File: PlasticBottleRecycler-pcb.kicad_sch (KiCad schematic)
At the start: 31 parts, among them J1 SWIM, J2 LCD, J3 Screw_Terminal_01x04, J4 NTC, J5 HEATER, J6 FAN1, J7 +12V, J8 +5V, Q1 IRF3205, Q2 BC337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

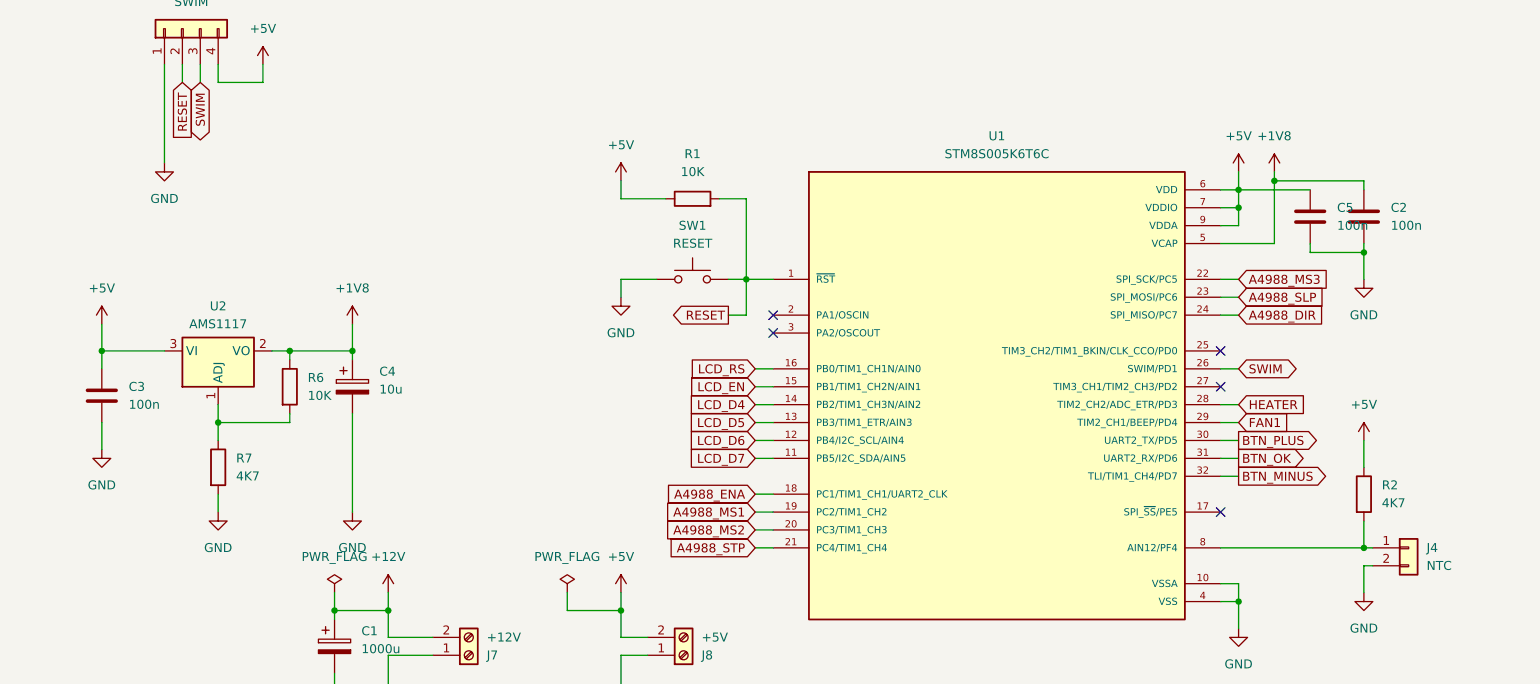
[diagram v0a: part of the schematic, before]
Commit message: Remove unnecesary voltage regulator
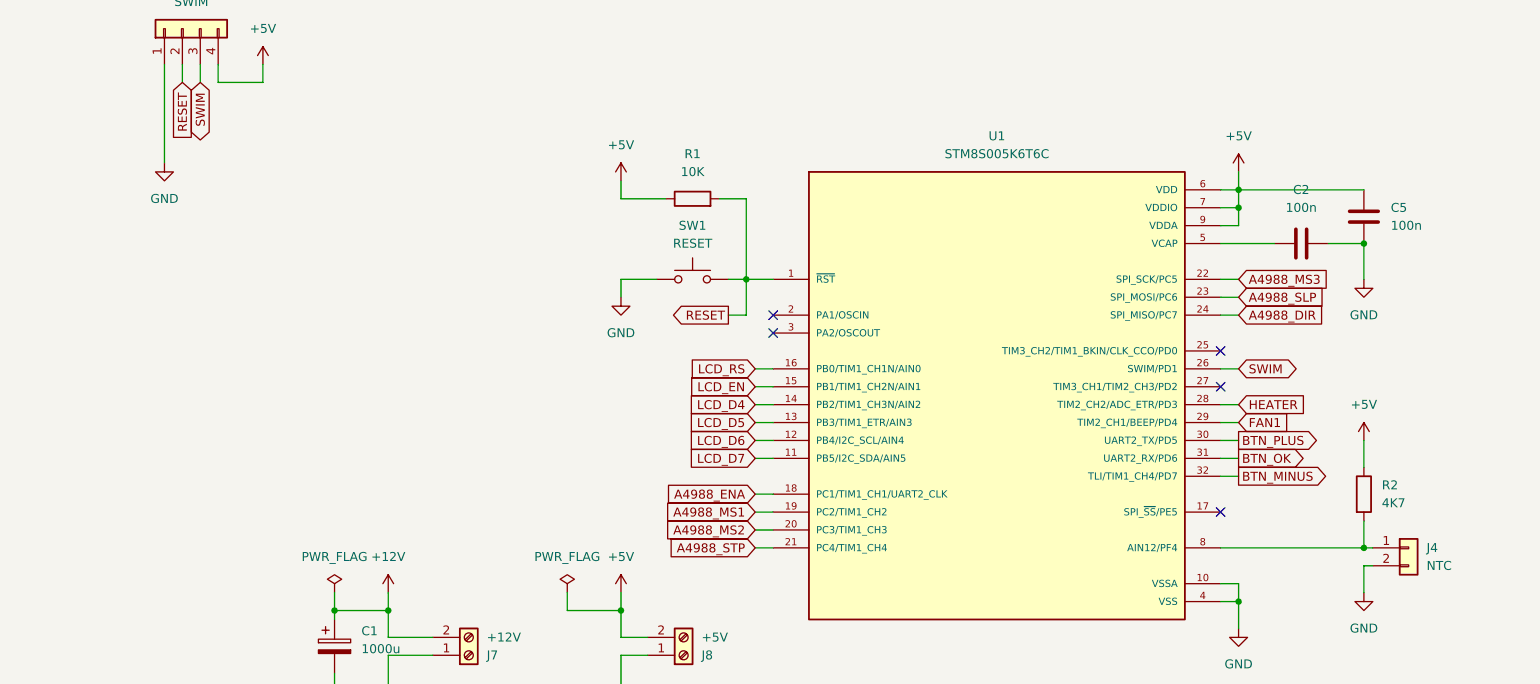
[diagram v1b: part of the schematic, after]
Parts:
- removed C3: 100n, Capacitor_THT:C_Disc_D6.0mm_W2.5mm_P5.00mm, symbol Device:C
- removed C4: 10u, Capacitor_THT:CP_Radial_D4.0mm_P2.00mm, symbol Device:C_Polarized
- removed R6: 10K, Resistor_THT:R_Axial_DIN0204_L3.6mm_D1.6mm_P5.08mm_Horizontal, symbol Device:R
- removed R7: 4K7, Resistor_THT:R_Axial_DIN0204_L3.6mm_D1.6mm_P5.08mm_Horizontal, symbol Device:R
- removed U2: AMS1117, Package_TO_SOT_SMD:SOT-223-3_TabPin2, symbol Regulator_Linear:AMS1117
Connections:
- net GND: now also C2.2; no longer C2.1
- net +1V8: no longer names the net of U1.5 (VCAP)
- net +1V8: now also C2.1; no longer C2.2
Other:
- moved on the sheet: C2, C5

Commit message: Revision 2.0
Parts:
- removed A1: Pololu_Breakout_A4988, Module:Pololu_Breakout-16_15.2x20.3mm, symbol Driver_Motor:Pololu_Breakout_A4988
- removed C1: 1000u, Capacitor_THT:CP_Radial_D10.0mm_P5.00mm, symbol Device:C_Polarized
- removed C2, C5: 100n, Capacitor_THT:C_Disc_D6.0mm_W2.5mm_P5.00mm, symbol Device:C
- removed J1: SWIM, Connector_PinHeader_2.54mm:PinHeader_1x04_P2.54mm_Vertical, symbol Connector_Generic:Conn_01x04
- removed J2: LCD, Connector_PinHeader_2.54mm:PinHeader_1x10_P2.54mm_Vertical, symbol Connector_Generic:Conn_01x10
- removed J3: Screw_Terminal_01x04, TerminalBlock:TerminalBlock_bornier-4_P5.08mm, symbol Connector:Screw_Terminal_01x04
- removed J4: NTC, Connector_JST:JST_XH_B2B-XH-A_1x02_P2.50mm_Vertical, symbol Connector_Generic:Conn_01x02
- removed J5: HEATER, TerminalBlock:TerminalBlock_bornier-2_P5.08mm, symbol Connector:Screw_Terminal_01x02
- removed J6: FAN1, Connector_PinHeader_2.54mm:PinHeader_1x02_P2.54mm_Vertical, symbol Connector_Generic:Conn_01x02
- removed J7: +12V, TerminalBlock:TerminalBlock_bornier-2_P5.08mm, symbol Connector:Screw_Terminal_01x02
- removed J8: +5V, TerminalBlock:TerminalBlock_bornier-2_P5.08mm, symbol Connector:Screw_Terminal_01x02
- removed Q1: IRF3205, PCM_Package_TO_SOT_THT_AKL:TO-220-3_Vertical_GDS, symbol PCM_Transistor_MOSFET_AKL:IRF3205
- removed Q2: BC337, PCM_Package_TO_SOT_THT_AKL:TO-92_Inline_Wide_CBE, symbol PCM_Transistor_BJT_AKL:BC337
- removed R1, R3, R4, R5: 10K, Resistor_THT:R_Axial_DIN0204_L3.6mm_D1.6mm_P5.08mm_Horizontal, symbol Device:R
- removed R2: 4K7, Resistor_THT:R_Axial_DIN0204_L3.6mm_D1.6mm_P5.08mm_Horizontal, symbol Device:R
- removed R8: 680, Resistor_THT:R_Axial_DIN0207_L6.3mm_D2.5mm_P10.16mm_Horizontal, symbol Device:R
- removed RV1: 100K, Potentiometer_THT:Potentiometer_Vishay_T73YP_Vertical, symbol Device:R_Potentiometer
- removed SW1: RESET, Button_Switch_THT:SW_PUSH_6mm_H5mm, symbol Switch:SW_Push
- removed SW2, SW3, SW4: SW_Push, Button_Switch_THT:SW_PUSH_6mm_H5mm, symbol Switch:SW_Push
- removed U1: STM8S005K6T6C, Package_QFP:LQFP-32_7x7mm_P0.8mm, symbol Extras:STM8S005K6T6C
- added J1, J3: Conn_01x08, Connector_Molex:Molex_KK-254_AE-6410-08A_1x08_P2.54mm_Vertical, symbol Connector_Generic:Conn_01x08
- added J2, J4: Conn_01x04, Connector_Molex:Molex_KK-254_AE-6410-04A_1x04_P2.54mm_Vertical, symbol Connector_Generic:Conn_01x04
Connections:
- new net Controller Board/+5V: J3.2 (Pin_2)
- new net Controller Board/BTN_MINUS: J4.4 (Pin_4)
- new net Controller Board/BTN_OK: J4.3 (Pin_3)
- new net Controller Board/BTN_PLUS: J4.2 (Pin_2)
- new net Controller Board/GND: J3.1 (Pin_1), J4.1 (Pin_1)
- new net Controller Board/LCD_D4: J3.6 (Pin_6)
- new net Controller Board/LCD_D5: J3.5 (Pin_5)
- new net Controller Board/LCD_D6: J3.4 (Pin_4)
- new net Controller Board/LCD_D7: J3.3 (Pin_3)
- new net Controller Board/LCD_EN: J3.7 (Pin_7)
- new net Controller Board/LCD_RS: J3.8 (Pin_8)
- new net IO Board/+5V: J1.2 (Pin_2)
- new net IO Board/BTN_MINUS: J2.4 (Pin_4)
- new net IO Board/BTN_OK: J2.3 (Pin_3)
- new net IO Board/BTN_PLUS: J2.2 (Pin_2)
- new net IO Board/GND: J1.1 (Pin_1), J2.1 (Pin_1)
- new net IO Board/LCD_D4: J1.6 (Pin_6)
- new net IO Board/LCD_D5: J1.5 (Pin_5)
- new net IO Board/LCD_D6: J1.4 (Pin_4)
- new net IO Board/LCD_D7: J1.3 (Pin_3)
- new net IO Board/LCD_EN: J1.7 (Pin_7)
- new net IO Board/LCD_RS: J1.8 (Pin_8)
- no-connect marks 5 -> 0
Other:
- added sheet Controller Board (ctrl_brd.kicad_sch)
- added sheet IO Board (io_brd.kicad_sch)
